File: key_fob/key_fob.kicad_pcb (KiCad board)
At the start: 2 copper layers, 20 parts, among them IC1 L4931ABDT33-TR, J1 Arduino-NANO-33, J2 B2B-PH-K-S_LF__SN_, U1 PS1240P02BT

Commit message: Got some stuff started for key fod pcb
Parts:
- moved C1 69.6 mm to (20.6, 47.4), turned to 90 degrees
- moved IC1 67.0 mm to (16.2, 41.5), turned to 180 degrees
- moved R6 52.0 mm to (38.7, 43.0), turned to 270 degrees
- moved U1 50.0 mm to (31.8, 54.7), turned to 270 degrees
- moved R5 47.2 mm to (44.0, 43.0), turned to 270 degrees
- moved J2 46.9 mm to (33.5, 35.0), turned to 180 degrees
- moved R4 41.3 mm to (49.1, 43.1), turned to 270 degrees
- moved D6 38.1 mm to (38.7, 48.2), turned to 90 degrees
- moved R2 37.8 mm to (66.5, 49.3), turned to 180 degrees
- moved R1 36.8 mm to (66.5, 56.5), turned to 180 degrees
- moved D5 36.5 mm to (44.0, 48.0), turned to 90 degrees
- moved C2 36.4 mm to (66.5, 83.1), turned to 180 degrees
- moved R3 35.9 mm to (54.4, 43.0), turned to 270 degrees
- moved S1 33.5 mm to (29.2, 43.3)
- moved D3 27.7 mm to (54.5, 47.9), turned to 90 degrees
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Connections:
- S1 pad 1: +BATT -> +3V3
- S1 pad 2: +3V3 -> +BATT
- S1 pad 5: LED_SW -> POWER_SW
- S1 pad 6: POWER_SW -> LED_SW

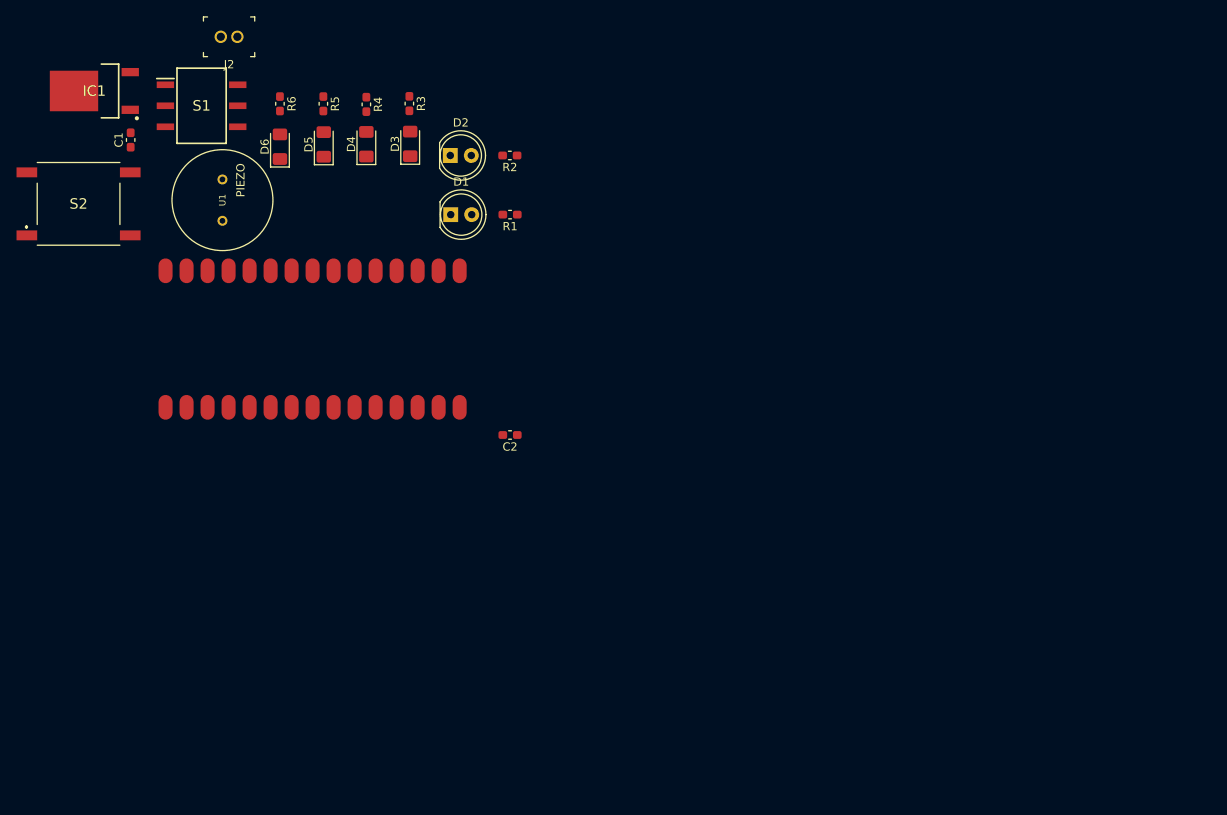
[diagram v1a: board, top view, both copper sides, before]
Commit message: First try at placing parts on PCB (no routing)
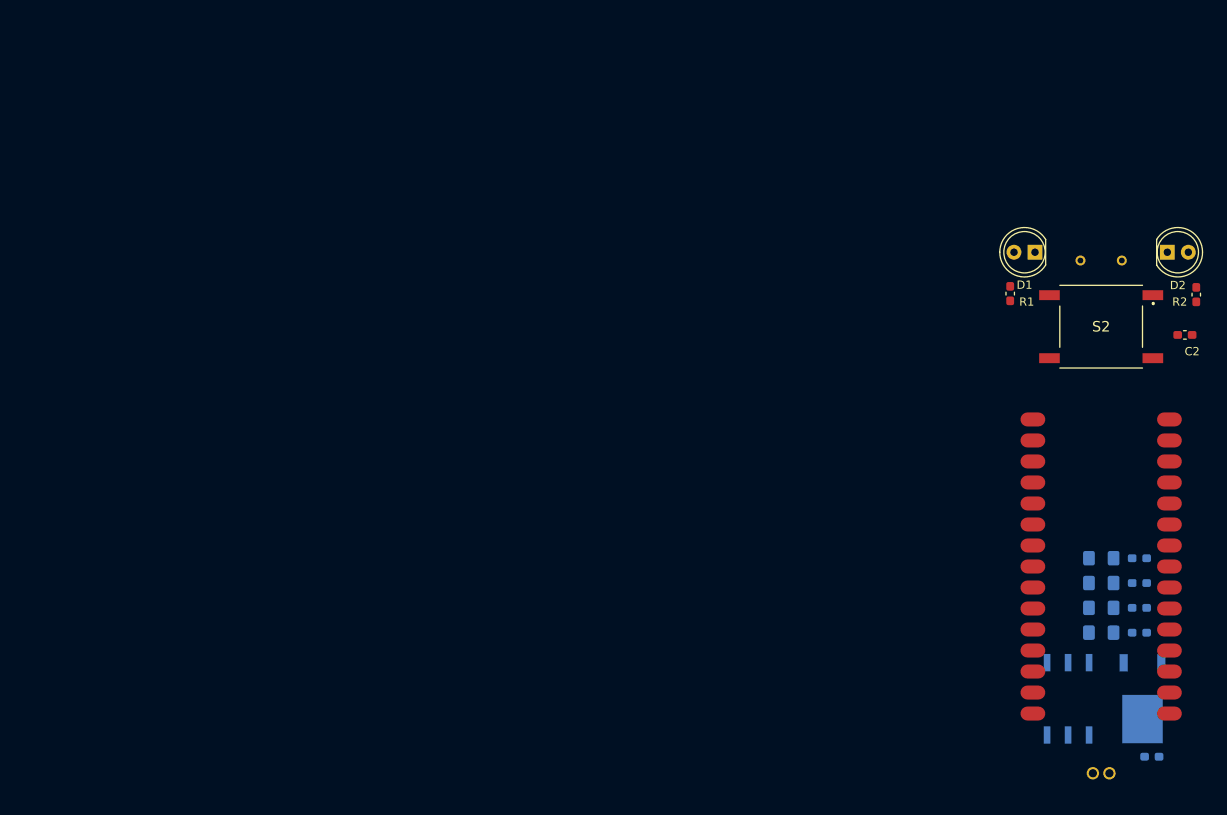
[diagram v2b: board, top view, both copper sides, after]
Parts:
- C1, D3, D4, D5, D6, IC1, J2, R3, R4, R5, R6, S1, U1: moved to B.Cu
- moved IC1 146.5 mm to (143.0, 115.0), turned to 270 degrees
- moved C1 144.2 mm to (144.1, 122.0), turned to 0 degrees
- moved J2 136.5 mm to (137.0, 124.0), turned to 0 degrees
- moved S1 127.0 mm to (134.0, 115.0), turned to 90 degrees
- moved S2 124.5 mm to (138.0, 70.0), turned to 0 degrees
- moved R6 122.0 mm to (142.6, 107.0), turned to 180 degrees
- moved R5 116.0 mm to (142.6, 104.0), turned to 180 degrees
- moved D6 115.4 mm to (138.0, 107.0), turned to 0 degrees
- moved R4 109.9 mm to (142.6, 101.0), turned to 180 degrees
- moved D5 109.4 mm to (138.0, 104.0), turned to 0 degrees
- moved U1 106.5 mm to (138.0, 62.0), turned to 180 degrees
- moved R3 104.0 mm to (142.6, 98.0), turned to 180 degrees
- moved D4 103.5 mm to (138.0, 101.0), turned to 0 degrees
- moved J1 99.2 mm to (138.0, 99.0), turned to 90 degrees
- moved D3 97.4 mm to (138.0, 98.0), turned to 0 degrees
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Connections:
- J1 pad 26: SPEAKER -> BUTTON0
- J1 pad 30: BUTTON0 -> SPEAKER
- S1 pad 2: +BATT -> POWER_SW
- S1 pad 5: POWER_SW -> +BATT

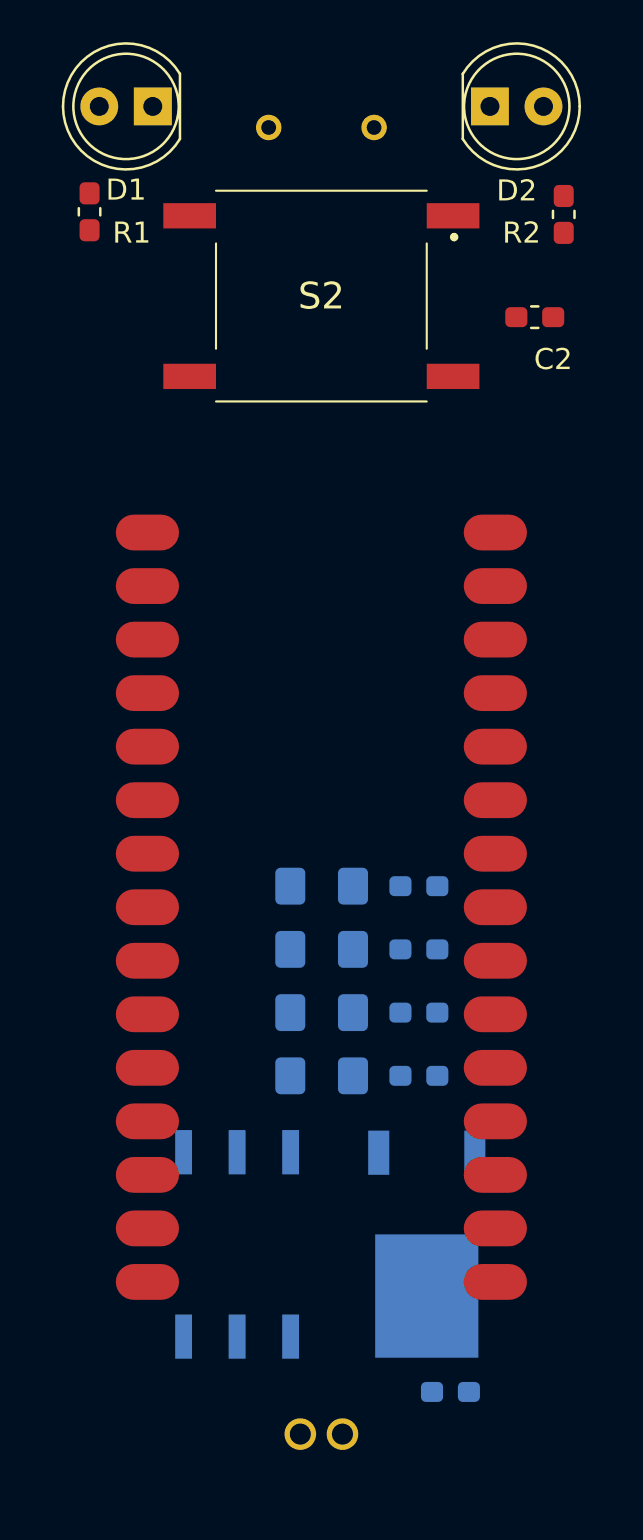
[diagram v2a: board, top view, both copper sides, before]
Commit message: Changed board size to 26x69mm
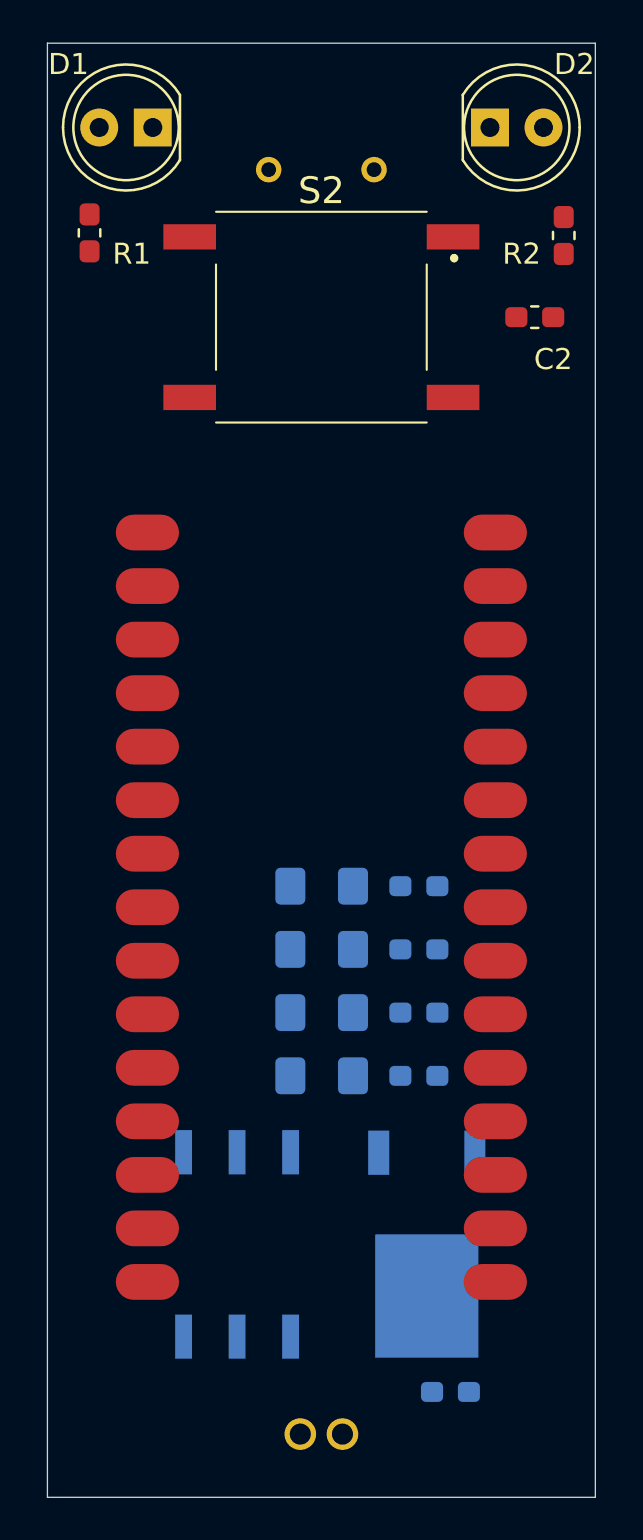
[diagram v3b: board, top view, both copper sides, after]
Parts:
- moved U1 2.00 mm to (138.0, 64.0)
- moved D1 1.00 mm to (130.0, 62.0)
- moved D2 1.00 mm to (146.0, 62.0)
- moved R1 1.00 mm to (127.0, 67.0)
- moved R2 1.00 mm to (149.5, 67.1)
- moved S2 1.00 mm to (138.0, 71.0)
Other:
- board outline added: 26 x 69 mm
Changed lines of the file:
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@@
   (general
     (thickness 1.6)
-    (drawings 0)
+    (drawings 4)
     (tracks 0)
     (zones 0)
@@
   )
   (module PS1240P02BT:PS1240P02BT (layer B.Cu)
-    (at 138 62 180)
-    (fp_text reference U1 (at 0 0) (layer B.SilkS)
-      (effects (font (size 0.787402 0.787402) (thickness 0.015)) (justify mirror))
+    (at 138 64 180)
+    (fp_text reference U1 (at -5 5) (layer B.SilkS)
+      (effects (font (size 0.787402 0.787402) (thickness 0.15)) (justify mirror))
     )
     (fp_text value PS1240P02BT (at 0 0) (layer B.Fab)
       (effects (font (size 0.787402 0.787402) (thickness 0.015)) (justify mirror))
     )
-    (fp_text user PIEZO (at 0 -2) (layer B.SilkS)
-      (effects (font (size 1.000488 1.000488) (thickness 0.015)) (justify mirror))
+    (fp_text user PIEZO (at 0 2) (layer B.SilkS)
+      (effects (font (size 1.000488 1.000488) (thickness 0.15)) (justify mirror))
     )
     (fp_circle (center 0 0) (end 6.10082 0) (layer B.SilkS) (width 0.127))
@@
   )
   (module SamacSys:3CSH9R (layer F.Cu)
-    (at 138 70)
+    (at 138 71)
     (descr 3CSH9R-2)
     (tags Switch)
     (attr smd)
-    (fp_text reference S2 (at 0 0) (layer F.SilkS)
+    (fp_text reference S2 (at 0 -6) (layer F.SilkS)
       (effects (font (size 1.27 1.27) (thickness 0.254)))
     )
@@
     (tags Switch)
     (attr smd)
-    (fp_text reference S1 (at 0 0 270) (layer B.SilkS)
+    (fp_text reference S1 (at 0 -6) (layer B.SilkS)
       (effects (font (size 1.27 1.27) (thickness 0.254)) (justify mirror))
     )
@@
   )
   (module Resistor_SMD:R_0603_1608Metric_Pad1.05x0.95mm_HandSolder (layer F.Cu)
-    (at 149.5 66.125 90)
+    (at 149.5 67.125 90)
     (descr "Resistor SMD 0603 (1608 Metric), square (rectangular) end terminal, IPC_7351 nominal with elongated pad for handsoldering. (Body size source: http://www.tortai-tech.com/upload/download/2011102023233369053.pdf), generated with kicad-footprint-generator")
     (tags "resistor handsolder")
@@
   )
   (module Resistor_SMD:R_0603_1608Metric_Pad1.05x0.95mm_HandSolder (layer F.Cu)
-    (at 127 66 90)
+    (at 127 67 90)
     (descr "Resistor SMD 0603 (1608 Metric), square (rectangular) end terminal, IPC_7351 nominal with elongated pad for handsoldering. (Body size source: http://www.tortai-tech.com/upload/download/2011102023233369053.pdf), generated with kicad-footprint-generator")
     (tags "resistor handsolder")
@@
     (at 137 124)
     (descr http://www.jst-mfg.com/product/pdf/eng/ePH.pdf)
-    (fp_text reference J2 (at 1 3.35) (layer B.SilkS)
+    (fp_text reference J2 (at -3 0) (layer B.SilkS)
       (effects (font (size 1 1) (thickness 0.15)) (justify mirror))
     )
@@
     (tags "Integrated Circuit")
     (attr smd)
-    (fp_text reference IC1 (at 0 0 270) (layer B.SilkS)
+    (fp_text reference IC1 (at -4 0) (layer B.SilkS)
       (effects (font (size 1.27 1.27) (thickness 0.254)) (justify mirror))
     )
@@
   )
   (module LED_THT:LED_D5.0mm (layer F.Cu)
-    (at 146 61)
+    (at 146 62)
     (descr "LED, diameter 5.0mm, 2 pins, http://cdn-reichelt.de/documents/datenblatt/A500/LL-504BC2E-009.pdf")
     (tags "LED diameter 5.0mm 2 pins")
-    (fp_text reference D2 (at 1.27 4) (layer F.SilkS)
+    (fp_text reference D2 (at 4 -3) (layer F.SilkS)
       (effects (font (size 1 1) (thickness 0.15)))
     )
@@
   )
   (module LED_THT:LED_D5.0mm (layer F.Cu)
-    (at 130 61 180)
+    (at 130 62 180)
     (descr "LED, diameter 5.0mm, 2 pins, http://cdn-reichelt.de/documents/datenblatt/A500/LL-504BC2E-009.pdf")
     (tags "LED diameter 5.0mm 2 pins")
-    (fp_text reference D1 (at 1.27 -3.96) (layer F.SilkS)
+    (fp_text reference D1 (at 4 3) (layer F.SilkS)
       (effects (font (size 1 1) (thickness 0.15)))
     )
@@
     )
   )
+  (gr_line (start 151 58) (end 125 58) (layer Edge.Cuts) (width 0.05))
+  (gr_line (start 151 127) (end 151 58) (layer Edge.Cuts) (width 0.05))
+  (gr_line (start 125 127) (end 151 127) (layer Edge.Cuts) (width 0.05))
+  (gr_line (start 125 58) (end 125 127) (layer Edge.Cuts) (width 0.05))
 )

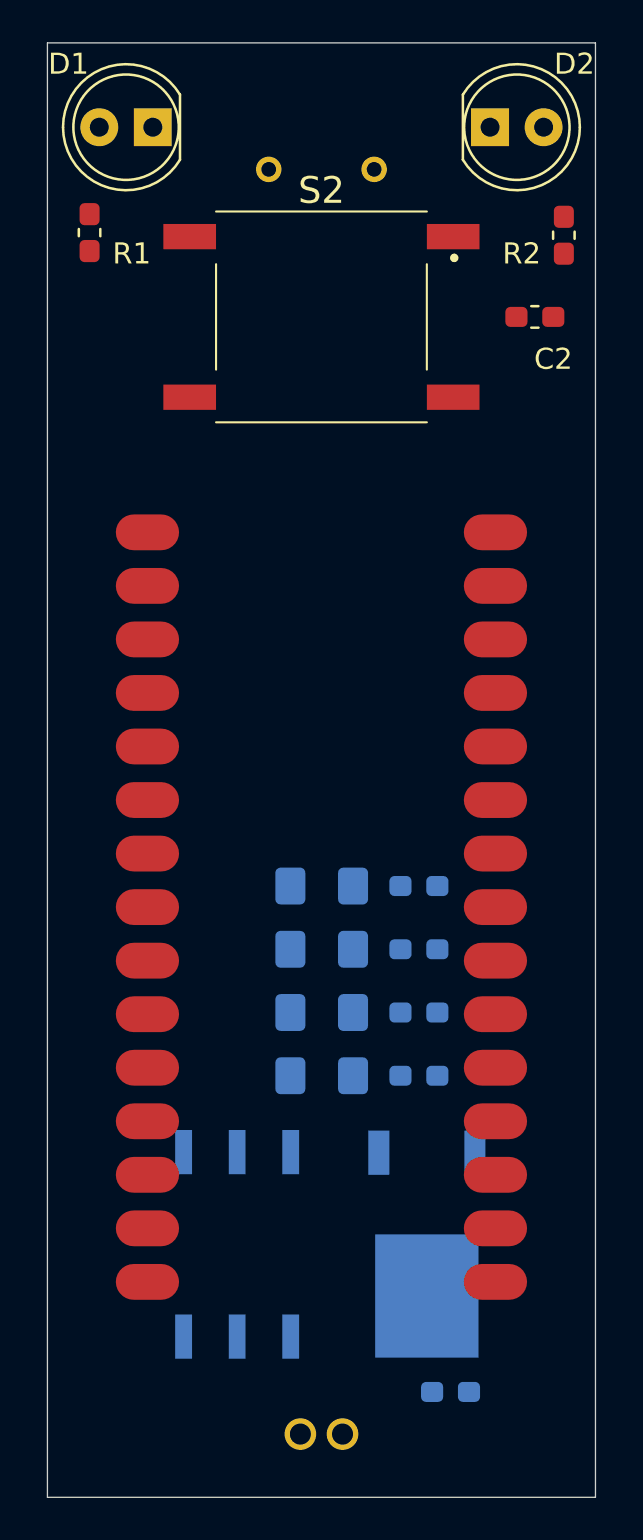
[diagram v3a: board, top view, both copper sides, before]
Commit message: Routed everything except the ground connections?=
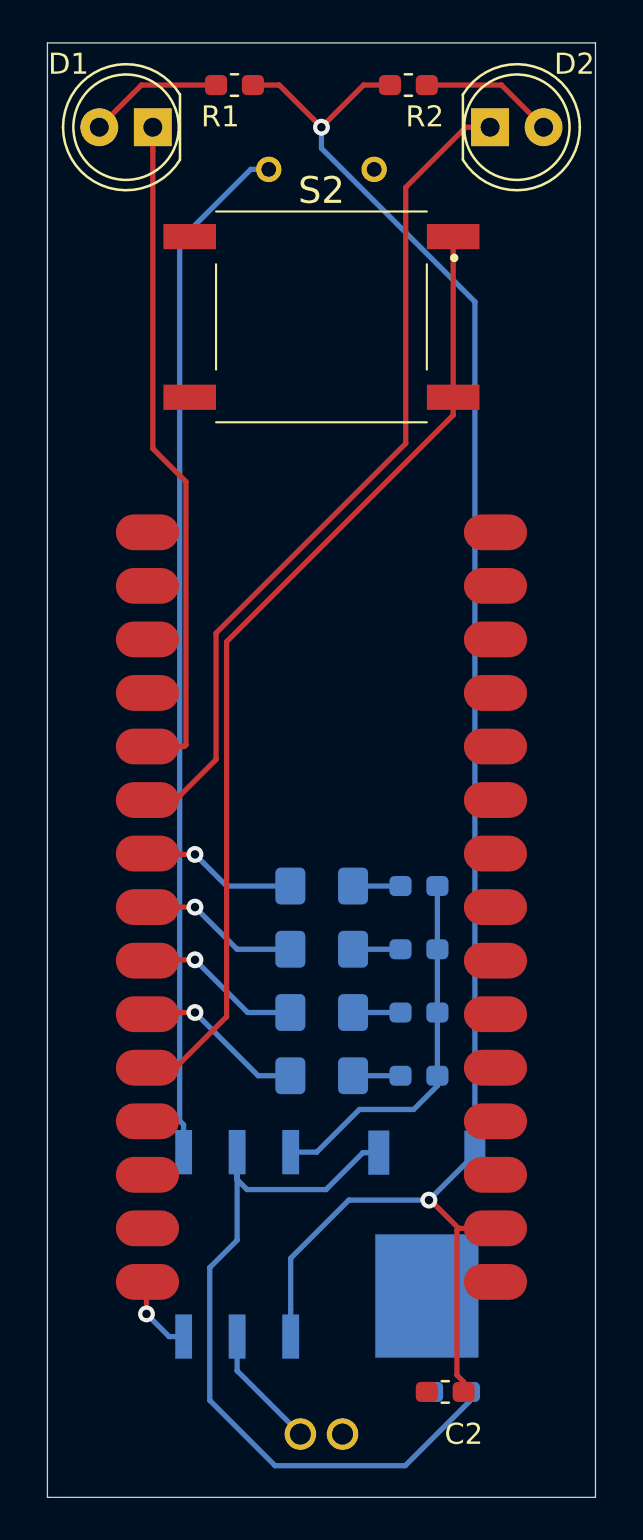
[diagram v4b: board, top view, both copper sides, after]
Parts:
- moved C2 51.2 mm to (143.9, 122.0)
- moved R2 10.3 mm to (142.1, 60.0), turned to 0 degrees
- moved R1 9.81 mm to (133.9, 60.0), turned to 180 degrees
- turned U1 to 0 degrees
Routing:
- net +3V3: track 0.00 -> 86.0 mm, vias 0 -> 2
- net SPEAKER_SW: track 0.00 -> 49.0 mm
- net BUTTON0: track 0.00 -> 46.2 mm
- net CONNECTED_LED: track 0.00 -> 40.1 mm
- net +BATT: track 0.00 -> 36.6 mm
- net POWER_LED: track 0.00 -> 31.8 mm
- net LED_SW: track 0.00 -> 17.7 mm
- net SPEAKER_LED: track 0.00 -> 8.06 mm, vias 0 -> 1
- net RECEIVE_LED: track 0.00 -> 7.83 mm, vias 0 -> 1
- net TRANSMIT_LED: track 0.00 -> 7.61 mm, vias 0 -> 1
- net HEARTBEAT_LED: track 0.00 -> 7.42 mm, vias 0 -> 1
- net Net-(D1-Pad2): track 0.00 -> 6.37 mm
- net Net-(D2-Pad2): track 0.00 -> 6.37 mm
- net POWER_SW: track 0.00 -> 5.87 mm
- net SPEAKER: track 0.00 -> 3.74 mm, vias 0 -> 1
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
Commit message: Cleaned up and mostly finished design
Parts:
- moved U1 0.20 mm to (138.0, 64.2)
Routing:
- net +3V3: track 86.0 -> 86.9 mm
- net CONNECTED_LED: track 40.1 -> 39.4 mm
- net GND: vias 0 -> 8
- added copper zone on B.Cu, net GND
- added copper zone on F.Cu, net GND
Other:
- board text added: "Made by Better Baby Buggies"
